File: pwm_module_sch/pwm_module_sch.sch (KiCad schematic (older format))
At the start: 15 parts

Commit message: schermatic
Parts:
- added C? (x2): 10uF, symbol Device:C
- added C? (x4): 0.1uF, symbol Device:C
- added C?: 1000uF, symbol Device:C_Polarized_US
- added D? (x3): ., symbol Device:D_Schottky_Dual_CommonCathode_AKA
- added D?: PESD1CAN, Package_TO_SOT_SMD:SOT-886, symbol Power_Protection:PESD3V3L4UF
- added J?: SWIMM, symbol Connector_Generic:Conn_01x01
- added R?: 0.1R, symbol Device:R
- added R?: 100k, symbol Device:R
- added R?: 10k, symbol Device:R
- added R?: 10R, symbol Device:R
- added U?: L78L33, Package_TO_SOT_SMD:SOT-89-3, symbol Regulator_Linear:L78L33_SOT89
- added U?: LM358, symbol Amplifier_Operational:LM358
- R? (x2): value R -> 100k
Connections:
- net +3V3: now also RV?.3, RV?.3, C?.1, C?.1, C?.1, C?.1, U?.1 (OUT), U?.4 (V-)
- net GND: now also RV?.1, RV?.1, SW?.1, C?.2, C?.2, C?.2, C?.2, C?.2, C?.2, C?.2, D?.1 (A), D?.1 (A), D?.2 (A), D?.3 (A), D?.3 (A), D?.5 (A), R?.2, R?.2, U?.2 (GND), U?.8 (V+)
- net at U?.17 (DIO): now also U?.11 (PB5)
- net at U?.18 (CLK): now also U?.12 (PB4)
- net at U?.10 (PA3): now also SW?.2
- net at U?.18 (PD1): now also J?.1 (Pin_1)
- net at U?.19 (PD2): now also U?.1, U?.2 (-)
- net at U?.2 (PD5): now also RV?.2
- net at U?.20 (PD3): now also U?.6 (-), U?.7
- net at U?.3 (PD6): now also RV?.2
- net +24V: now reaches R?.1
- net +24V: now also Q?.3 (S), C?.1, D?.2 (K), R?.2; no longer Q?.2 (D)
- net at U?.3 (+): now also R?.1, R?.2
- net at U?.5 (+): now also R?.1
- new net: C?.1, C?.1, D?.1 (K1), R?.1, U?.3 (IN)
- new net +VSW: Q?.2 (D), R?.1
- new net AC: D?.1 (A), D?.2 (K), D?.2 (K), D?.3 (A)
- no-connect marks 5 -> 12
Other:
- moved on the sheet: C?, D?, Q?, R?, RV?, SW?, U?, U?A, U?B

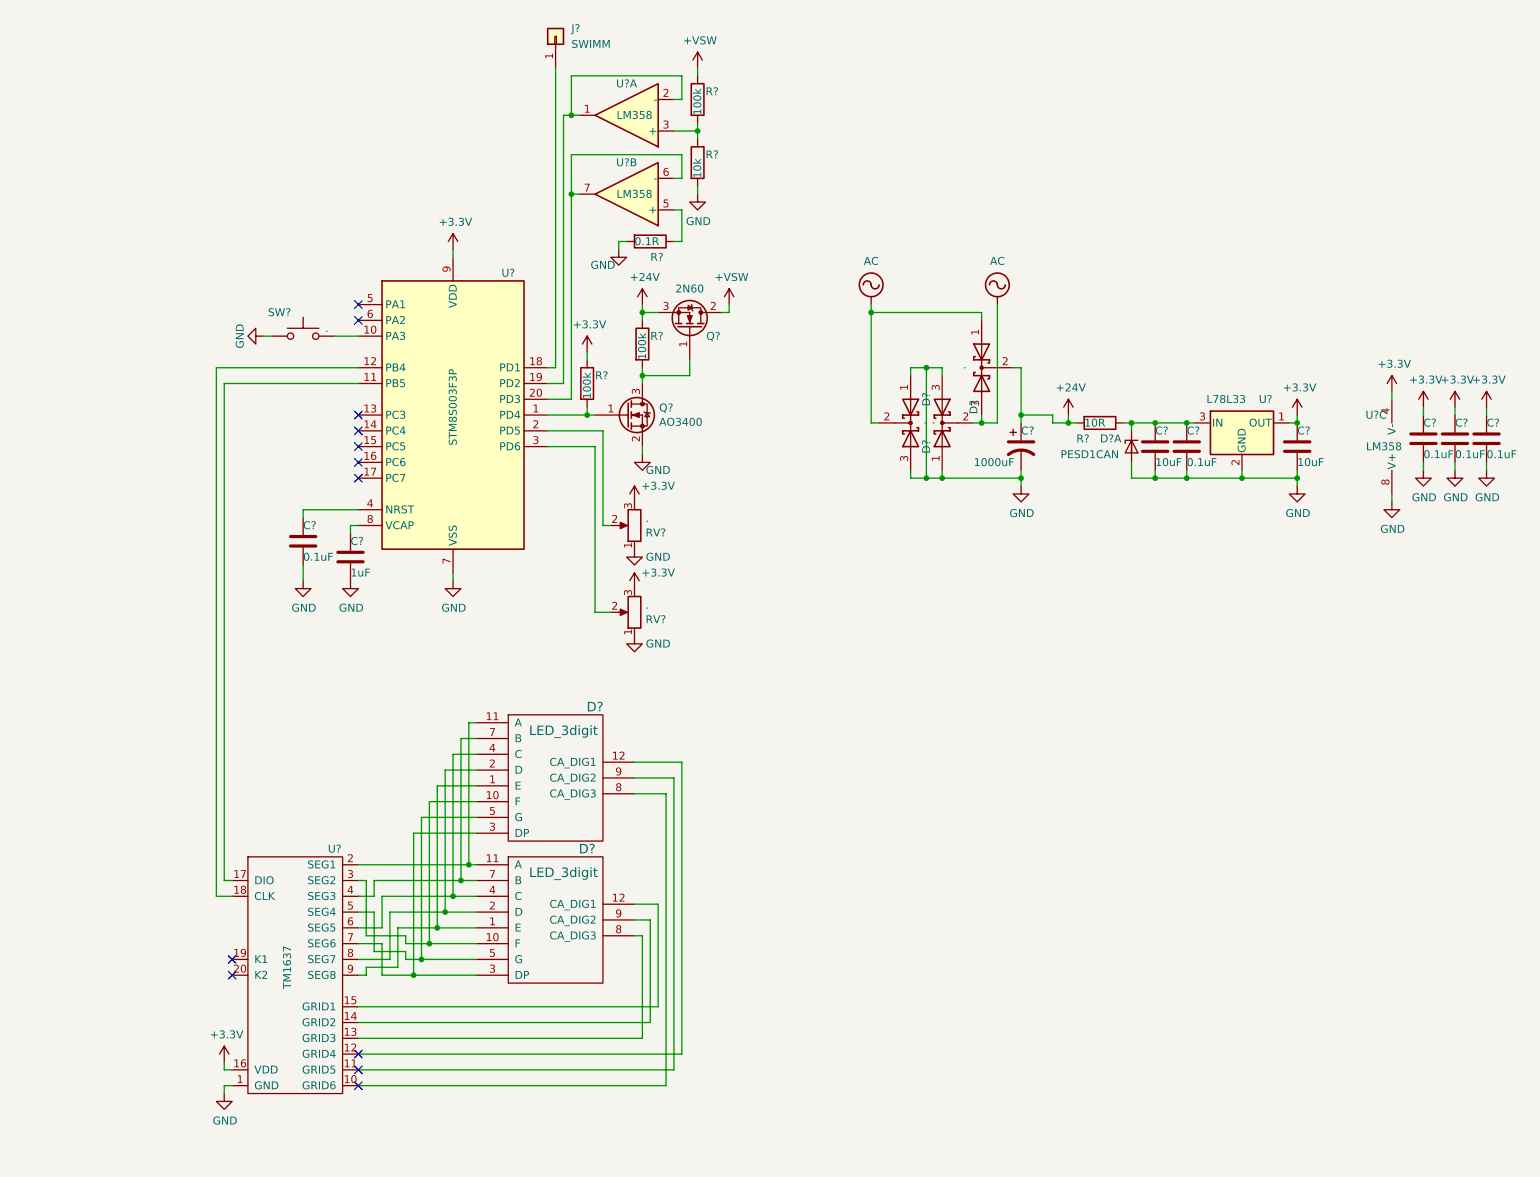
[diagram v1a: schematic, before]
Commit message: clock on func, pcb assignment
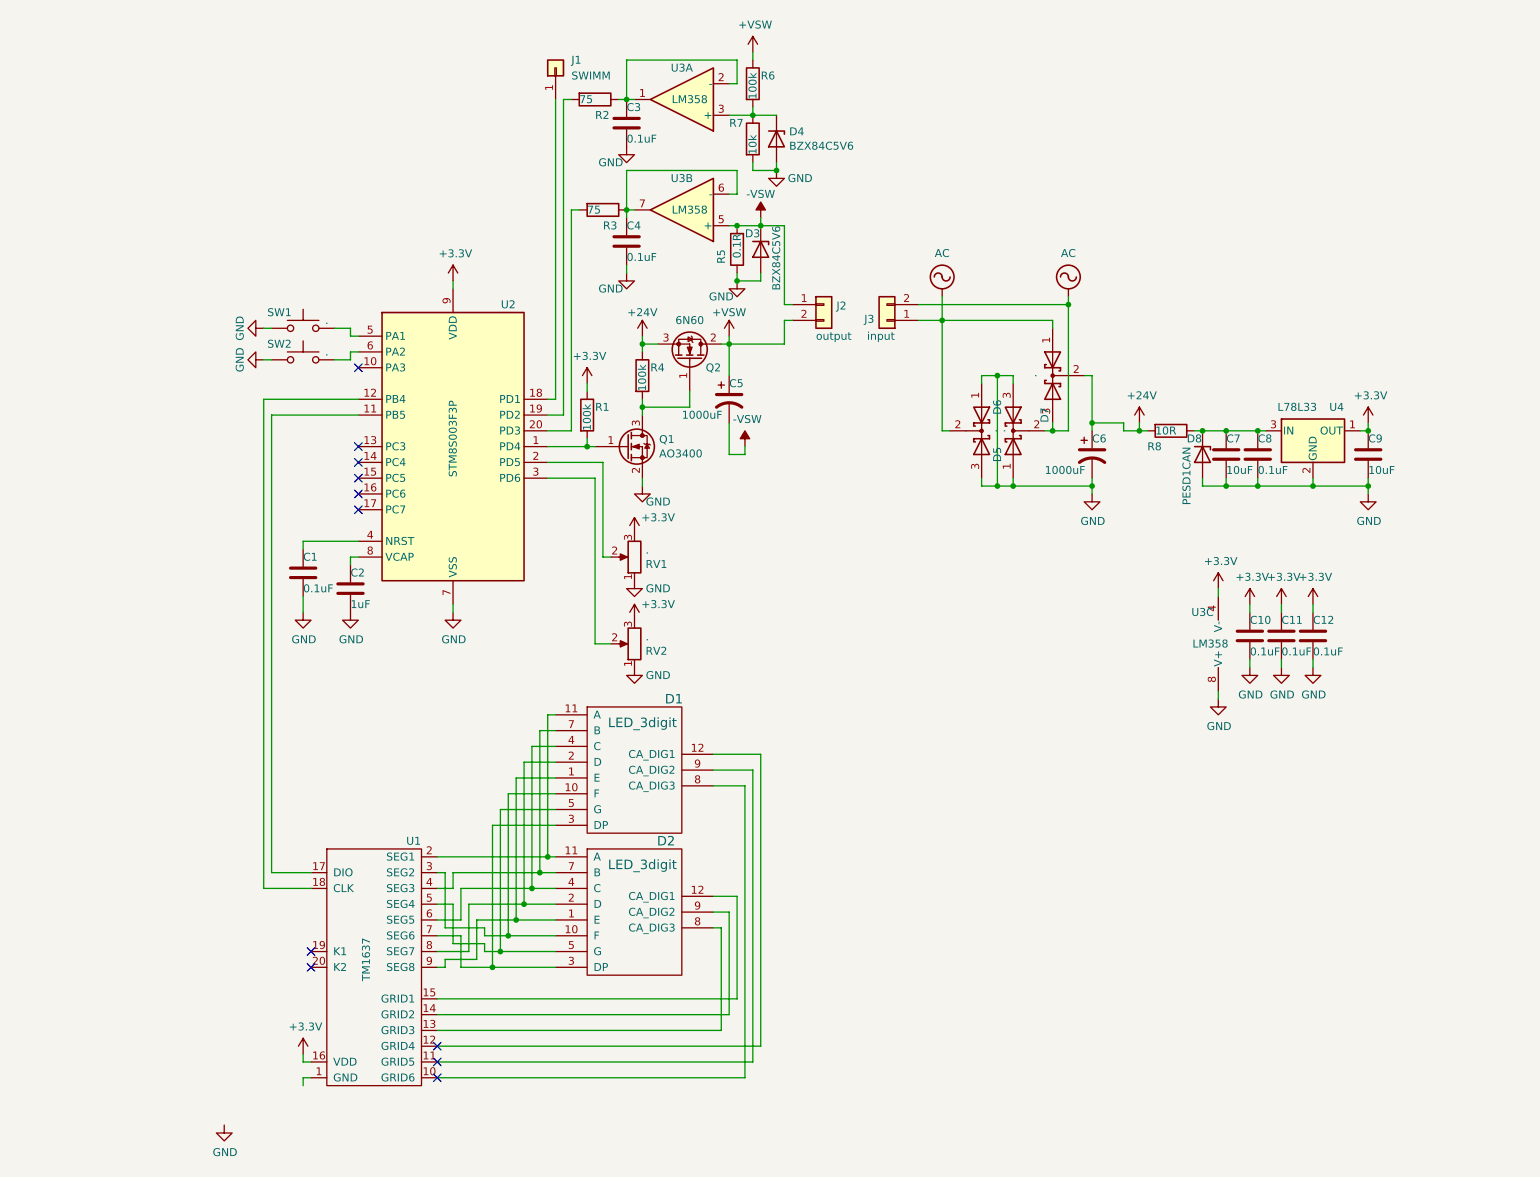
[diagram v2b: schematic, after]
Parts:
- removed D?: PESD1CAN, Package_TO_SOT_SMD:SOT-886, symbol Power_Protection:PESD3V3L4UF
- added C3, C4: 0.1uF, Capacitor_SMD:C_0805_2012Metric, symbol Device:C
- added C5: 1000uF, Capacitor_THT:CP_Radial_D5.0mm_P2.00mm, symbol Device:C_Polarized_US
- added D3, D4: BZX84C5V6, Package_TO_SOT_SMD:SOT-23, symbol Diode:BZX84Cxx
- added D8: PESD1CAN, Package_TO_SOT_SMD:SOT-23, symbol Diode:BZX84Cxx
- added J2: output, Connector_Wire:SolderWire-1sqmm_1x02_P7.8mm_D1.4mm_OD3.9mm, symbol Connector_Generic:Conn_01x02
- added J3: input, Connector_Wire:SolderWire-1sqmm_1x02_P7.8mm_D1.4mm_OD3.9mm, symbol Connector_Generic:Conn_01x02
- added R2, R3: 75, Resistor_SMD:R_0402_1005Metric, symbol Device:R
- added SW1: ., Button_Switch_THT:SW_PUSH_6mm, symbol Switch:SW_Push
- C1, C10, C11, C12, C2, C7, C8, C9: renamed from C?; footprint (none) -> Capacitor_SMD:C_0805_2012Metric
- C6: renamed from C?; footprint (none) -> Capacitor_THT:CP_Radial_D5.0mm_P2.00mm
- D1, D2: renamed from D?; footprint (none) -> pwm_module:FYT-3631
- D5, D6, D7: renamed from D?; footprint (none) -> Package_TO_SOT_THT:TO-220-3_Vertical
- J1: renamed from J?; footprint (none) -> Connector_Wire:SolderWirePad_1x01_SMD_1x2mm
- Q1: renamed from Q?; footprint (none) -> Package_TO_SOT_SMD:SOT-23
- Q2: renamed from Q?; value 2N60 -> 6N60; footprint TO_SOT_Packages_THT:TO-92_Molded_Narrow -> Package_TO_SOT_THT:TO-220-3_Vertical
- R1, R4: renamed from R?; footprint (none) -> Resistor_SMD:R_0402_1005Metric
- R5: renamed from R?; footprint (none) -> Resistor_SMD:R_1210_3225Metric
- R6, R7, R8: renamed from R?; footprint (none) -> Resistor_SMD:R_0805_2012Metric
- RV1, RV2: renamed from RV?; footprint (none) -> pwm_module:SP3-4
- SW2: renamed from SW?; footprint (none) -> Button_Switch_THT:SW_PUSH_6mm
- U1: renamed from U?; footprint (none) -> Package_SO:SOIC-20W_7.5x12.8mm_P1.27mm
- U3: renamed from U?; footprint (none) -> Package_SO:SO-8_3.9x4.9mm_P1.27mm
- gave numbers to parts that had none: 2
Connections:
- net +VSW: now also C5.1, J2.2 (Pin_2)
- net AC: now also J3.1 (Pin_1), J3.2 (Pin_2)
- net GND: now also R5.1, C3.2, C4.2, D3.2 (A), D4.2 (A), D8.2 (A), SW1.1; no longer R5.2, U1.1 (GND)
- net at U2.10 (PA3): no longer SW2.2
- net at U3.1, U3.2 (-): now also C3.1, R2.1; no longer U2.19 (PD2)
- net at U3.6 (-), U3.7: now also C4.1, R3.1; no longer U2.20 (PD3)
- net at U2.5 (PA1): now also SW1.2
- net at U2.6 (PA2): now also SW2.2
- net -VSW: now reaches U3.5 (+)
- net -VSW: now also R5.2, C5.2, D3.1 (K), J2.1 (Pin_1); no longer R5.1
- net at R6.2, R7.1, U3.3 (+): now also D4.1 (K)
- net at C7.1, C8.1, R8.1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: now also D8.1 (K)
- new net: R2.2, U2.19 (PD2)
- new net: R3.2, U2.20 (PD3)
- no-connect marks 12 -> 11
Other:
- moved on the sheet: C1, C10, C11, C12, C2, C6, C7, C8, C9, D1, D2, D5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

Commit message: one-layer PCB 6x6cm
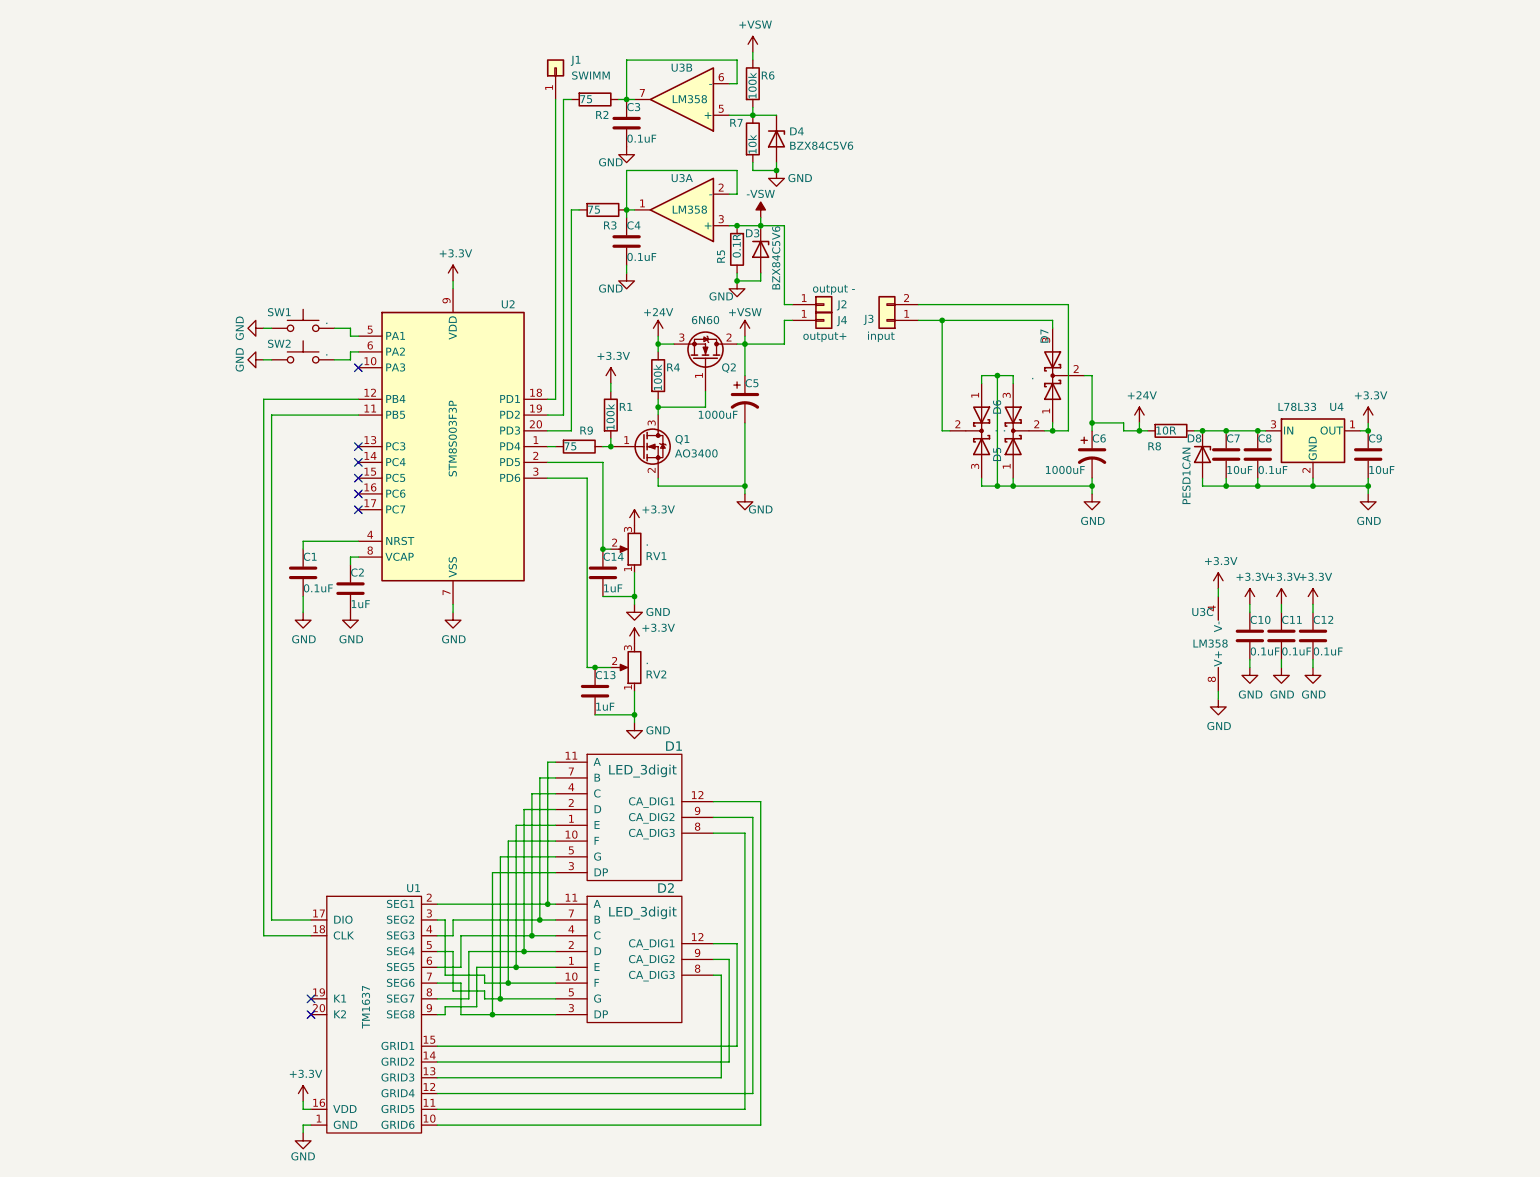
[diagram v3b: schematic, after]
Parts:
- removed J2: output, Connector_Wire:SolderWire-1sqmm_1x02_P7.8mm_D1.4mm_OD3.9mm, symbol Connector_Generic:Conn_01x02
- added C13, C14: 1uF, Capacitor_SMD:C_0805_2012Metric, symbol Device:C
- added J2: output -, Connector_Wire:SolderWire-2.5sqmm_1x01_D2.4mm_OD4.4mm, symbol Connector_Generic:Conn_01x01
- added J4: output+, Connector_Wire:SolderWire-2.5sqmm_1x01_D2.4mm_OD4.4mm, symbol Connector_Generic:Conn_01x01
- added R9: 75, Resistor_SMD:R_1206_3216Metric, symbol Device:R
- D3, D4, D8: footprint Package_TO_SOT_SMD:SOT-23 -> Diode_SMD:D_SOT-23_ANK
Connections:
- net +VSW: now also J4.1 (Pin_1)
- net -VSW: now also U3.3 (+), J2.1 (Pin_1); no longer C5.2, U3.5 (+)
- net GND: now also C5.2, U1.1 (GND), C13.2, C14.2
- net at U1.10 (GRID6): now also D1.12 (CA_DIG1); no longer D1.8 (CA_DIG3)
- net at U1.11 (GRID5): now also D1.8 (CA_DIG3); no longer D1.9 (CA_DIG2)
- net at U1.12 (GRID4): now also D1.9 (CA_DIG2); no longer D1.12 (CA_DIG1)
- net at Q1.1 (G), R1.2: now also R9.1; no longer U2.1 (PD4)
- net at RV1.2, U2.2 (PD5): now also C14.1
- net at RV2.2, U2.3 (PD6): now also C13.1
- net at D4.1 (K), R6.2, R7.1: now also U3.5 (+); no longer U3.3 (+)
- net at C3.1, R2.1: now also U3.6 (-), U3.7; no longer U3.1, U3.2 (-)
- net at C4.1, R3.1: now also U3.1, U3.2 (-); no longer U3.6 (-), U3.7
- net AC: no longer names the net of D5.2 (K), D7.3 (A), J3.1 (Pin_1)
- net AC: no longer D6.2 (K), D7.1 (A), J3.2 (Pin_2)
- new net: R9.2, U2.1 (PD4)
- new net: D6.2 (K), D7.1 (A), J3.2 (Pin_2)
- no-connect marks 11 -> 8
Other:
- moved on the sheet: C5, D1, D2, Q1, Q2, R1, R4, RV1, RV2, U1

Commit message: tm adapt, pwm add
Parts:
- added R10, R11: 100k, Resistor_SMD:R_0402_1005Metric, symbol Device:R
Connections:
- net +3V3: now also R10.1, R11.1
- net at U1.17 (DIO), U2.11 (PB5): now also R11.2
- net at U1.18 (CLK), U2.12 (PB4): now also R10.2
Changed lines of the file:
@@
 	2400 4300 2400 4200
-Wire Wire Line
-	2150 6350 2450 6350
-Wire Wire Line
-	2200 6250 2450 6250
 Wire Wire Line
 	2200 3050 2750 3050
@@
 	5200 3550 5200 3500
 Connection ~ 5200 3500
+$Comp
+L Device:R R11
+U 1 1 620D8C1B
+P 2400 6050
+F 0 "R11" H 2400 6200 50  0000 L CNN
+F 1 "100k" V 2400 5950 50  0000 L CNN
+F 2 "Resistor_SMD:R_0402_1005Metric" V 2330 6050 50  0001 C CNN
+F 3 "~" H 2400 6050 50  0001 C CNN
+	1    2400 6050
+	1    0    0    -1
+$EndComp
+$Comp
+L Device:R R10
+U 1 1 620DFA0D
+P 2300 6050
+F 0 "R10" H 2200 6200 50  0000 L CNN
+F 1 "100k" V 2300 5950 50  0000 L CNN
+F 2 "Resistor_SMD:R_0402_1005Metric" V 2230 6050 50  0001 C CNN
+F 3 "~" H 2300 6050 50  0001 C CNN
+	1    2300 6050
+	1    0    0    -1
+$EndComp
+$Comp
+L power:+3.3V #PWR0116
+U 1 1 620E41A7
+P 2300 5800
+F 0 "#PWR0116" H 2300 5650 50  0001 C CNN
+F 1 "+3.3V" H 2450 5900 50  0000 C CNN
+F 2 "" H 2300 5800 50  0001 C CNN
+F 3 "" H 2300 5800 50  0001 C CNN
+	1    2300 5800
+	1    0    0    -1
+$EndComp
+Wire Wire Line
+	2400 5900 2400 5850
+Wire Wire Line
+	2400 5850 2300 5850
+Connection ~ 2300 5850
+Wire Wire Line
+	2300 5800 2300 5850
+Wire Wire Line
+	2150 6350 2300 6350
+Wire Wire Line
+	2300 6200 2300 6350
+Connection ~ 2300 6350
+Wire Wire Line
+	2300 6350 2450 6350
+Wire Wire Line
+	2200 6250 2400 6250
+Wire Wire Line
+	2400 6200 2400 6250
+Connection ~ 2400 6250
+Wire Wire Line
+	2400 6250 2450 6250
+Wire Wire Line
+	2300 5900 2300 5850
 $EndSCHEMATC
